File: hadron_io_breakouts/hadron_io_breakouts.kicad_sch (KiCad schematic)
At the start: 15 parts, among them J1 TF38-18S-0.5SV_830_, J2 SFM-110-02-L-D-A, J3 TF38-18S-0.5SV_830_, J4 SAMTEC-SFM-120-02-L-D-A, J5 SM04B-NSHSS-TB_LF__SN_, J6 SM08B-NSHSS-TB LFSN, J7 Conn_01x03_Pin

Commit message: Minor updates to controller, 3rd stab at hadron breakout
Minor updates to controller and firmware to make labels more consistent. Took another try at the hadron IO breakout. Old manufacture files removed.
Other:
- note added: "Differential Pair Routing for OSH Park 4 Layer properties 90 ohm impedence 1 oz copper 7.87 mil (0.1999) FR408HR 2113 dk 3.61 9.84 mil spacing (0.25 mm) 13.39 mil trace width (0.3401 mm)"
- note added: "GPIO10 and GPIO11 have both pull-up and pull-down resistors. Only populate one or the other based on your application."
- note added: "SBC Debug UART 3.3v logic level"
- note added: "SBC GPIOs"
- note added: "SBC/MCU Serial IO"
- note removed: "Differential Pair Routing for Easy PCB 4 Layer properties 90 ohm impedence 1 oz copper 14.1 mil dielectric 8 mil spacing (0.2032 mm) dielectric constant 4.5 trace width: 0.4256 mm"
- moved on the sheet: J4, J5, J6, J7, R1, R2, R3, R4, R5, R6, R7, R8

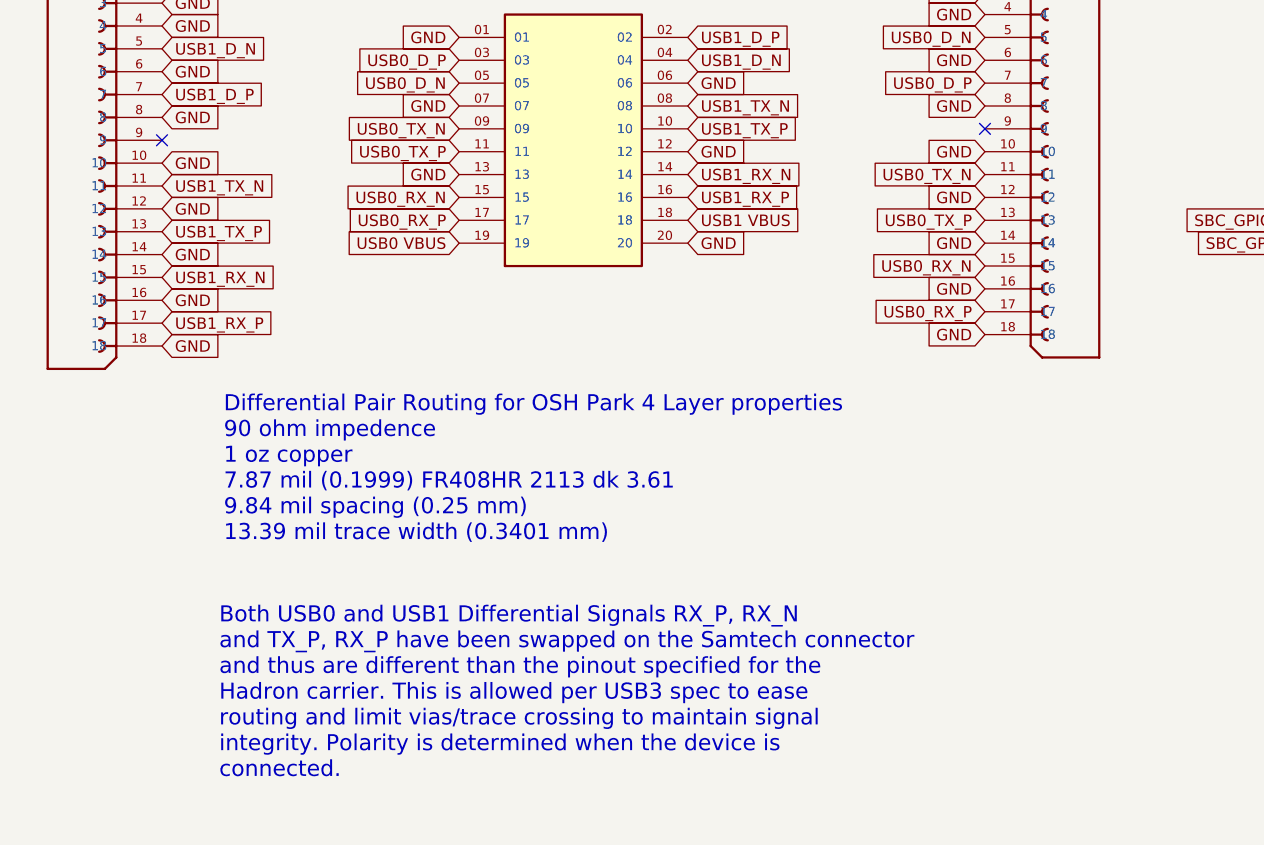
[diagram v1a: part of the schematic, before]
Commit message: Updated hadron_io_breakout with <ahem> differential crossover
Fixed issue where I wasn't crossing over SS differential lines. Still need to review prior to manufacture.
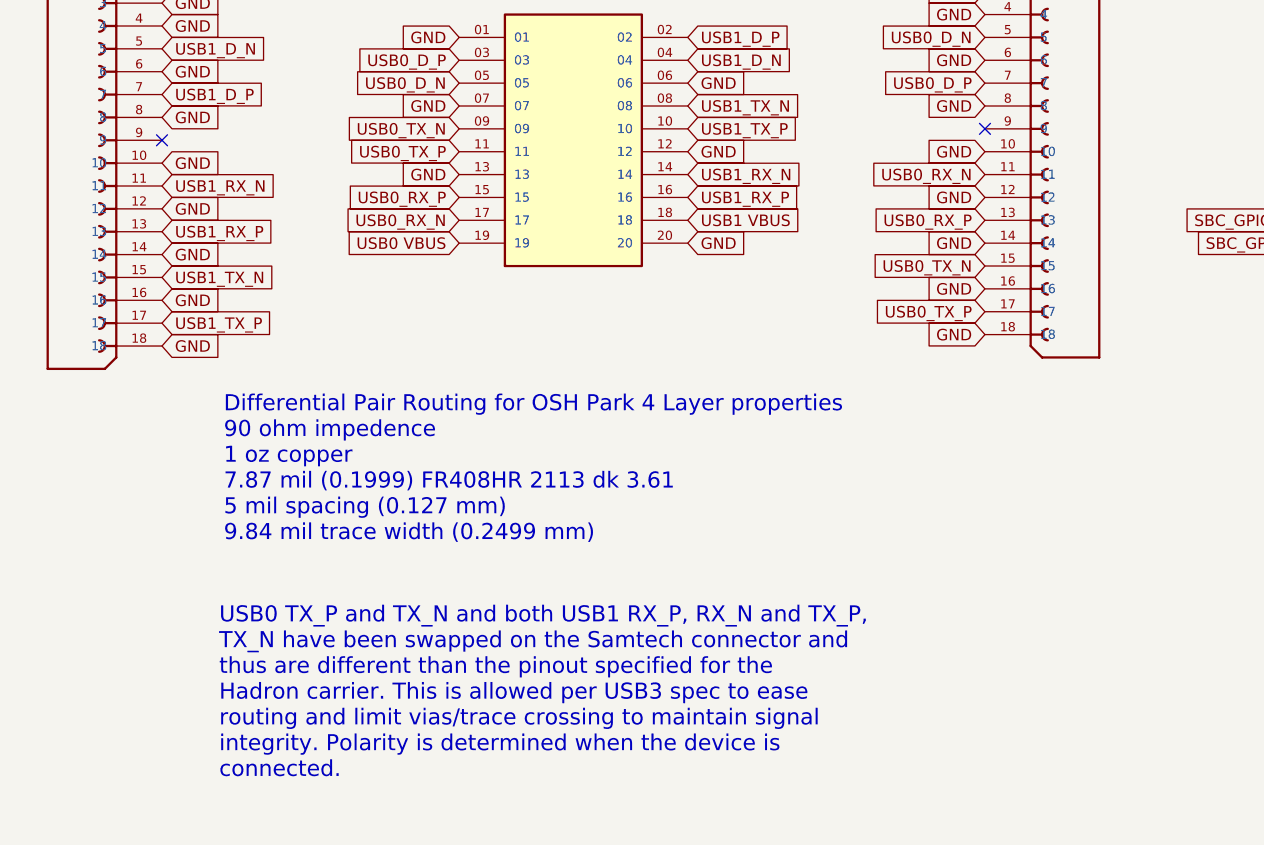
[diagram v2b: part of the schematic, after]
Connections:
- net USB0_RX_N: now also J2.17, J3.11; no longer J2.15, J3.15
- net USB0_RX_P: now also J2.15, J3.13; no longer J2.17, J3.17
- net USB0_TX_N: now also J3.15; no longer J3.11
- net USB0_TX_P: now also J3.17; no longer J3.13
- net USB1_RX_N: now also J1.11; no longer J1.15
- net USB1_RX_P: now also J1.13; no longer J1.17
- net USB1_TX_N: now also J1.15; no longer J1.11
- net USB1_TX_P: now also J1.17; no longer J1.13
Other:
- note added: "Differential Pair Routing for OSH Park 4 Layer properties 90 ohm impedence 1 oz copper 7.87 mil (0.1999) FR408HR 2113 dk 3.61 5 mil spacing (0.127 mm) 9.84 mil trace width (0.2499 mm)"
- note added: "USB0 TX_P and TX_N and both USB1 RX_P, RX_N and TX_P, TX_N have been swapped on the Samtech connector and thus are different than the pinout specified for the Hadron carrier. This is allowed per USB3 spec to ease routing and limit vias/trace crossing to maintain signal integrity. Polarity is determined when the device is connected."
- note removed: "Both USB0 and USB1 Differential Signals RX_P, RX_N and TX_P, RX_P have been swapped on the Samtech connector and thus are different than the pinout specified for the Hadron carrier. This is allowed per USB3 spec to ease routing and limit vias/trace crossing to maintain signal integrity. Polarity is determined when the device is connected."
- note removed: "Differential Pair Routing for OSH Park 4 Layer properties 90 ohm impedence 1 oz copper 7.87 mil (0.1999) FR408HR 2113 dk 3.61 9.84 mil spacing (0.25 mm) 13.39 mil trace width (0.3401 mm)"
